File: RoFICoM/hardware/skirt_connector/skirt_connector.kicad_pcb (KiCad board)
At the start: 2 copper layers, 25 x 25 mm, 17 parts, among them J1 Cable, J10 SENSE_1, J11 SENSE_2, J12 48V_B, J13 48V_2, J14 GND_B, J15 GND_2, J16 RX_B, J17 TX_2, J2 48V_A, J3 48V_1, J4 GND_A, J5 GND_1, J6 RX_A, J7 TX_1, J8 SENSE_A, J9 SENSE_B

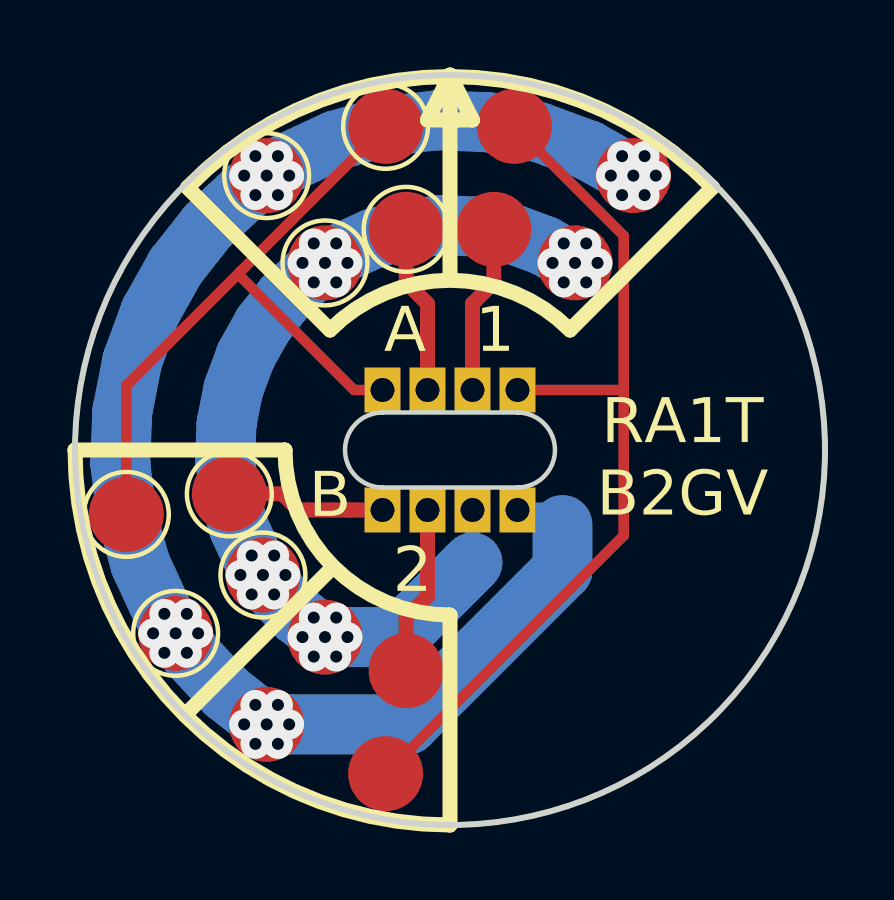
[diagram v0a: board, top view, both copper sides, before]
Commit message: RoFICoM: Add version 0.2 of the skirt PCB
- add VL53L1X distance sensor
- use flat ribbon cable for connection to the control board
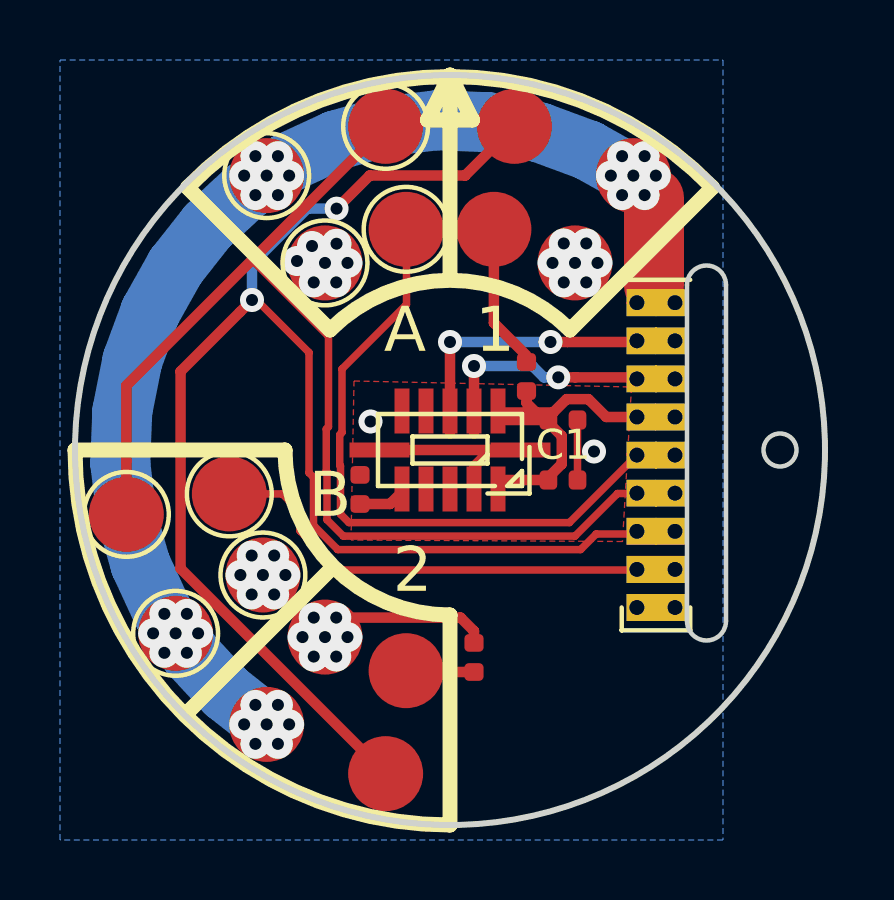
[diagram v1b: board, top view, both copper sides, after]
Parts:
- added C1: 470n, Capacitor_SMD:C_0402_1005Metric, F.Cu at (153.8, 101.0)
- added C2: 100n, Capacitor_SMD:C_0402_1005Metric, F.Cu at (153.8, 99.0)
- added R1: 10k, Resistor_SMD:R_0402_1005Metric, F.Cu at (147.0, 101.3)
- added R2: 10k, Resistor_SMD:R_0402_1005Metric, F.Cu at (152.6, 97.5)
- added R3: 10k, Resistor_SMD:R_0402_1005Metric, F.Cu at (150.8, 106.9)
- added U1: VL53L1X, rofi:VL53L1X_handsoldering, F.Cu at (150.0, 100.0)
- J1: footprint rofi:skirt_8_pin -> rofi:flat_cable_9
- moved J1 9.15 mm to (157.5, 105.2), turned to 90 degrees
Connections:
- J1 pad 1: RX -> GND
- J1 pad 2: S_A_PIN -> S_B_PIN
- J1 pad 3: S_1_PAD -> TX
- J1 pad 4: TX -> RX
- J1 pad 5: 48V -> S_A_PIN
- J1 pad 6: GND -> +3V3
- J1 pad 7: S_2_PAD -> SCL
- J1 pad 8: S_B_PIN -> SDA
- J10 pad 1: S_1_PAD -> Net-(J10-Pad1)
- J11 pad 1: S_2_PAD -> Net-(J11-Pad1)
- J12 pad 1: 48V -> +48V
- J13 pad 1: 48V -> +48V
- J2 pad 1: 48V -> +48V
- J3 pad 1: 48V -> +48V
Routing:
- net 48V: track 49.8 -> 0.00 mm, vias 28 -> 0
- net +48V: track 0.00 -> 40.2 mm, vias 0 -> 28
- net TX: track 29.9 -> 52.5 mm, vias 0 -> 2
- net GND: track 31.2 -> 13.3 mm, vias 28 -> 30
- net S_A_PIN: track 5.65 -> 22.8 mm
- net RX: track 23.0 -> 38.8 mm
- net +3V3: track 0.00 -> 13.0 mm
- net S_B_PIN: track 5.33 -> 17.5 mm
- net SDA: track 0.00 -> 11.7 mm, vias 0 -> 2
- net SCL: track 0.00 -> 10.3 mm, vias 0 -> 2
- net S_1_PAD: track 5.65 -> 0.00 mm
- net S_2_PAD: track 5.65 -> 0.00 mm
- net Net-(J10-Pad1): track 0.00 -> 4.66 mm
- net Net-(J11-Pad1): track 0.00 -> 2.40 mm
- net Net-(R1-Pad1): track 0.00 -> 1.57 mm
- added copper zone on B.Cu, net GND
- added copper zone on F.Cu, net GND
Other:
- outline, holes or cut-outs redrawn
- board text removed: "RA1T B2GV"

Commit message: RoFICoM: Update skirt connector label
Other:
- board text added: "RoFICoM Skirt v0.2 03/2019"
- board text removed: "RoFI - DockSkirt v0.1 12/2018"
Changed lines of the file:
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@@
   (gr_line (start 157.9 94.5) (end 157.9 105.7) (layer Edge.Cuts) (width 0.15))
   (gr_arc (start 158.55 94.5) (end 159.2 94.5) (angle -180) (layer Edge.Cuts) (width 0.15))
-  (gr_text "RoFI - DockSkirt\nv0.1    12/2018" (at 150.25 105.5) (layer B.SilkS)
+  (gr_text "RoFICoM Skirt\nv0.2 03/2019" (at 146.55 100.15) (layer B.SilkS)
     (effects (font (size 1.5 1.5) (thickness 0.3)) (justify mirror))
   )

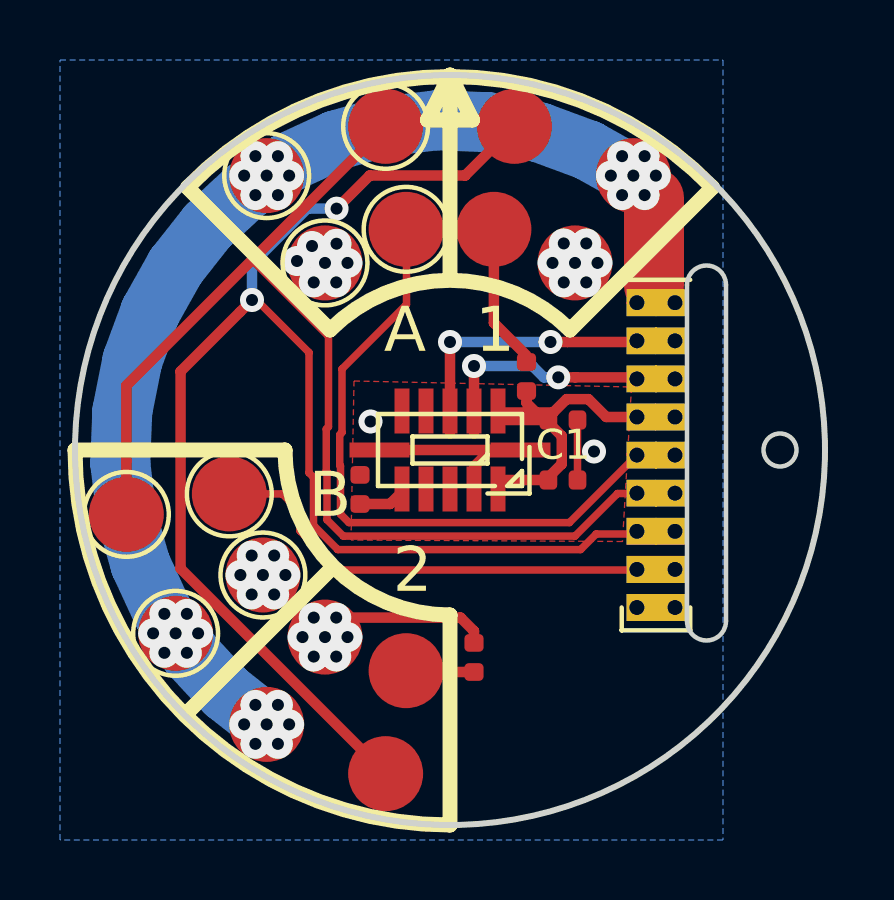
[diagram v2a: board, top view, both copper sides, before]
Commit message: RoFICoM: Add missing order codes for the skirt connector
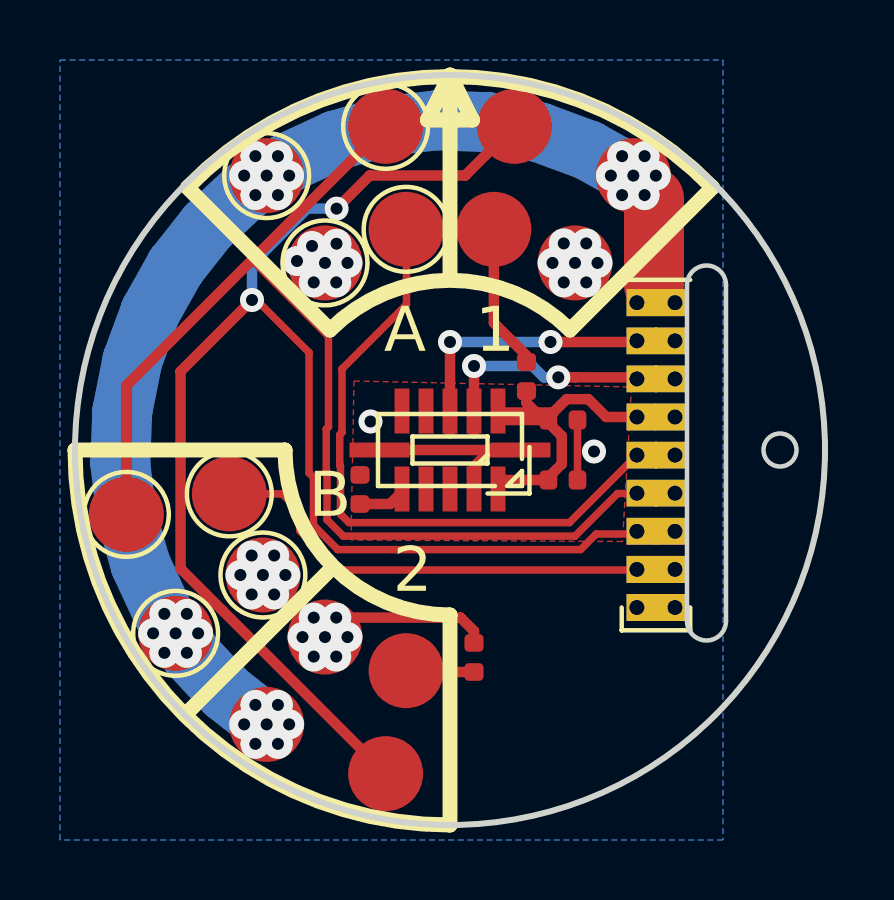
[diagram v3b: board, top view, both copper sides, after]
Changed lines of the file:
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@@
-(kicad_pcb (version 20171130) (host pcbnew 5.0.2-bee76a0~70~ubuntu18.04.1)
+(kicad_pcb (version 20171130) (host pcbnew 5.1.0-060a0da~80~ubuntu18.04.1)
   (general
     (thickness 1.6)
@@
   )
   (setup
-    (last_trace_width 0.35)
+    (last_trace_width 0.25)
     (user_trace_width 0.35)
     (user_trace_width 0.5)
@@
     (zone_45_only no)
     (trace_min 0.2)
-    (segment_width 0.5)
-    (edge_width 0.15)
     (via_size 0.8)
     (via_drill 0.4)
@@
     (uvia_min_size 0.2)
     (uvia_min_drill 0.1)
+    (edge_width 0.15)
+    (segment_width 0.5)
     (pcb_text_width 0.3)
     (pcb_text_size 1.5 1.5)
@@
     (tags capacitor)
     (attr smd)
-    (fp_text reference C1 (at 0 -1.17) (layer F.SilkS)
+    (fp_text reference C1 (at 0 -1.17) (layer F.SilkS) hide
       (effects (font (size 1 1) (thickness 0.15)))
     )
@@
   (gr_arc (start 147.039376 97.633074) (end 138.843834 107.400141) (angle -35) (layer Eco1.User) (width 0.2))
   (gr_arc (start 147.039376 97.633074) (end 137.272309 89.437532) (angle -35) (layer Eco1.User) (width 0.2))
-  (via (at 143.888727 109.146165) (size 1) (layers F.Cu B.Cu) (net 6))
-  (via (at 144.638727 109.146165) (size 1) (layers F.Cu B.Cu) (net 6))
-  (via (at 144.263727 109.795684) (size 1) (layers F.Cu B.Cu) (net 6))
-  (via (at 143.513727 109.795684) (size 1) (layers F.Cu B.Cu) (net 6))
-  (via (at 143.138727 109.146165) (size 1) (layers F.Cu B.Cu) (net 6))
-  (via (at 143.513727 108.496645) (size 1) (layers F.Cu B.Cu) (net 6))
-  (via (at 144.263727 108.496645) (size 1) (layers F.Cu B.Cu) (net 6))
-  (via (at 140.853834 106.111272) (size 1) (layers F.Cu B.Cu) (net 6))
-  (via (at 141.603834 106.111272) (size 1) (layers F.Cu B.Cu) (net 6))
-  (via (at 141.228834 106.760791) (size 1) (layers F.Cu B.Cu) (net 6))
-  (via (at 140.478834 106.760791) (size 1) (layers F.Cu B.Cu) (net 6))
-  (via (at 140.103834 106.111272) (size 1) (layers F.Cu B.Cu) (net 6))
-  (via (at 140.478834 105.461752) (size 1) (layers F.Cu B.Cu) (net 6))
-  (via (at 141.228834 105.461752) (size 1) (layers F.Cu B.Cu) (net 6))
-  (via (at 156.111272 90.853834) (size 1) (layers F.Cu B.Cu) (net 6))
-  (via (at 156.861272 90.853834) (size 1) (layers F.Cu B.Cu) (net 6))
-  (via (at 156.486272 91.503353) (size 1) (layers F.Cu B.Cu) (net 6))
-  (via (at 155.736272 91.503353) (size 1) (layers F.Cu B.Cu) (net 6))
-  (via (at 155.361272 90.853834) (size 1) (layers F.Cu B.Cu) (net 6))
-  (via (at 155.736272 90.204314) (size 1) (layers F.Cu B.Cu) (net 6))
-  (via (at 156.486272 90.204314) (size 1) (layers F.Cu B.Cu) (net 6))
-  (via (at 143.888727 90.853834) (size 1) (layers F.Cu B.Cu) (net 6))
-  (via (at 144.638727 90.853834) (size 1) (layers F.Cu B.Cu) (net 6))
-  (via (at 144.263727 91.503353) (size 1) (layers F.Cu B.Cu) (net 6))
-  (via (at 143.513727 91.503353) (size 1) (layers F.Cu B.Cu) (net 6))
-  (via (at 143.138727 90.853834) (size 1) (layers F.Cu B.Cu) (net 6))
-  (via (at 143.513727 90.204314) (size 1) (layers F.Cu B.Cu) (net 6))
-  (via (at 144.263727 90.204314) (size 1) (layers F.Cu B.Cu) (net 6))
-  (segment (start 156.111272 90.853834) (end 154.605257 90.010425) (width 2) (layer B.Cu) (net 6))
-  (segment (start 154.605257 90.010425) (end 152.985844 89.412992) (width 2) (layer B.Cu) (net 6))
-  (segment (start 152.985844 89.412992) (end 151.292911 89.076246) (width 2) (layer B.Cu) (net 6))
-  (segment (start 151.292911 89.076246) (end 149.568142 89.00848) (width 2) (layer B.Cu) (net 6))
-  (segment (start 149.568142 89.00848) (end 147.854006 89.211361) (width 2) (layer B.Cu) (net 6))
-  (segment (start 147.854006 89.211361) (end 146.192712 89.679895) (width 2) (layer B.Cu) (net 6))
-  (segment (start 146.192712 89.679895) (end 144.625166 90.402543) (width 2) (layer B.Cu) (net 6))
-  (segment (start 144.625166 90.402543) (end 143.189966 91.361513) (width 2) (layer B.Cu) (net 6))
-  (segment (start 143.189966 91.361513) (end 141.922452 92.533191) (width 2) (layer B.Cu) (net 6))
-  (segment (start 141.922452 92.533191) (end 140.853834 93.888727) (width 2) (layer B.Cu) (net 6))
-  (segment (start 140.853834 93.888727) (end 140.010425 95.394742) (width 2) (layer B.Cu) (net 6))
-  (segment (start 140.010425 95.394742) (end 139.412992 97.014155) (width 2) (layer B.Cu) (net 6))
-  (segment (start 139.076246 98.707088) (end 139.00848 100.431857) (width 2) (layer B.Cu) (net 6))
-  (segment (start 139.00848 100.431857) (end 139.211361 102.145993) (width 2) (layer B.Cu) (net 6))
-  (segment (start 139.211361 102.145993) (end 139.679895 103.807287) (width 2) (layer B.Cu) (net 6))
-  (segment (start 139.679895 103.807287) (end 140.402543 105.374833) (width 2) (layer B.Cu) (net 6))
-  (segment (start 140.402543 105.374833) (end 141.361513 106.810033) (width 2) (layer B.Cu) (net 6))
-  (segment (start 141.361513 106.810033) (end 142.533191 108.077547) (width 2) (layer B.Cu) (net 6))
-  (segment (start 142.533191 108.077547) (end 143.888727 109.146165) (width 2) (layer B.Cu) (net 6))
-  (segment (start 139.412992 97.014155) (end 139.076246 98.707088) (width 2) (layer B.Cu) (net 6))
   (via (at 145.833223 106.236022) (size 1) (layers F.Cu B.Cu) (net 1))
   (via (at 146.583223 106.236022) (size 1) (layers F.Cu B.Cu) (net 1))
@@
   (segment (start 152.145993 89.211361) (end 150.507354 90.85) (width 0.35) (layer F.Cu) (net 5))
   (segment (start 150.507354 90.85) (end 147.323891 90.85) (width 0.35) (layer F.Cu) (net 5))
+  (via (at 143.888727 109.146165) (size 1) (layers F.Cu B.Cu) (net 6))
+  (via (at 144.638727 109.146165) (size 1) (layers F.Cu B.Cu) (net 6))
+  (via (at 144.263727 109.795684) (size 1) (layers F.Cu B.Cu) (net 6))
+  (via (at 143.513727 109.795684) (size 1) (layers F.Cu B.Cu) (net 6))
+  (via (at 143.138727 109.146165) (size 1) (layers F.Cu B.Cu) (net 6))
+  (via (at 143.513727 108.496645) (size 1) (layers F.Cu B.Cu) (net 6))
+  (via (at 144.263727 108.496645) (size 1) (layers F.Cu B.Cu) (net 6))
+  (via (at 140.853834 106.111272) (size 1) (layers F.Cu B.Cu) (net 6))
+  (via (at 141.603834 106.111272) (size 1) (layers F.Cu B.Cu) (net 6))
+  (via (at 141.228834 106.760791) (size 1) (layers F.Cu B.Cu) (net 6))
+  (via (at 140.478834 106.760791) (size 1) (layers F.Cu B.Cu) (net 6))
+  (via (at 140.103834 106.111272) (size 1) (layers F.Cu B.Cu) (net 6))
+  (via (at 140.478834 105.461752) (size 1) (layers F.Cu B.Cu) (net 6))
+  (via (at 141.228834 105.461752) (size 1) (layers F.Cu B.Cu) (net 6))
+  (via (at 156.111272 90.853834) (size 1) (layers F.Cu B.Cu) (net 6))
+  (via (at 156.861272 90.853834) (size 1) (layers F.Cu B.Cu) (net 6))
+  (via (at 156.486272 91.503353) (size 1) (layers F.Cu B.Cu) (net 6))
+  (via (at 155.736272 91.503353) (size 1) (layers F.Cu B.Cu) (net 6))
+  (via (at 155.361272 90.853834) (size 1) (layers F.Cu B.Cu) (net 6))
+  (via (at 155.736272 90.204314) (size 1) (layers F.Cu B.Cu) (net 6))
+  (via (at 156.486272 90.204314) (size 1) (layers F.Cu B.Cu) (net 6))
+  (via (at 143.888727 90.853834) (size 1) (layers F.Cu B.Cu) (net 6))
+  (via (at 144.638727 90.853834) (size 1) (layers F.Cu B.Cu) (net 6))
+  (via (at 144.263727 91.503353) (size 1) (layers F.Cu B.Cu) (net 6))
+  (via (at 143.513727 91.503353) (size 1) (layers F.Cu B.Cu) (net 6))
+  (via (at 143.138727 90.853834) (size 1) (layers F.Cu B.Cu) (net 6))
+  (via (at 143.513727 90.204314) (size 1) (layers F.Cu B.Cu) (net 6))
+  (via (at 144.263727 90.204314) (size 1) (layers F.Cu B.Cu) (net 6))
+  (segment (start 156.111272 90.853834) (end 154.605257 90.010425) (width 2) (layer B.Cu) (net 6))
+  (segment (start 154.605257 90.010425) (end 152.985844 89.412992) (width 2) (layer B.Cu) (net 6))
+  (segment (start 152.985844 89.412992) (end 151.292911 89.076246) (width 2) (layer B.Cu) (net 6))
+  (segment (start 151.292911 89.076246) (end 149.568142 89.00848) (width 2) (layer B.Cu) (net 6))
+  (segment (start 149.568142 89.00848) (end 147.854006 89.211361) (width 2) (layer B.Cu) (net 6))
+  (segment (start 147.854006 89.211361) (end 146.192712 89.679895) (width 2) (layer B.Cu) (net 6))
+  (segment (start 146.192712 89.679895) (end 144.625166 90.402543) (width 2) (layer B.Cu) (net 6))
+  (segment (start 144.625166 90.402543) (end 143.189966 91.361513) (width 2) (layer B.Cu) (net 6))
+  (segment (start 143.189966 91.361513) (end 141.922452 92.533191) (width 2) (layer B.Cu) (net 6))
+  (segment (start 141.922452 92.533191) (end 140.853834 93.888727) (width 2) (layer B.Cu) (net 6))
+  (segment (start 140.853834 93.888727) (end 140.010425 95.394742) (width 2) (layer B.Cu) (net 6))
+  (segment (start 140.010425 95.394742) (end 139.412992 97.014155) (width 2) (layer B.Cu) (net 6))
+  (segment (start 139.076246 98.707088) (end 139.00848 100.431857) (width 2) (layer B.Cu) (net 6))
+  (segment (start 139.00848 100.431857) (end 139.211361 102.145993) (width 2) (layer B.Cu) (net 6))
+  (segment (start 139.211361 102.145993) (end 139.679895 103.807287) (width 2) (layer B.Cu) (net 6))
+  (segment (start 139.679895 103.807287) (end 140.402543 105.374833) (width 2) (layer B.Cu) (net 6))
+  (segment (start 140.402543 105.374833) (end 141.361513 106.810033) (width 2) (layer B.Cu) (net 6))
+  (segment (start 141.361513 106.810033) (end 142.533191 108.077547) (width 2) (layer B.Cu) (net 6))
+  (segment (start 142.533191 108.077547) (end 143.888727 109.146165) (width 2) (layer B.Cu) (net 6))
+  (segment (start 139.412992 97.014155) (end 139.076246 98.707088) (width 2) (layer B.Cu) (net 6))
   (segment (start 156.23 95.09) (end 156.8 94.52) (width 0.7) (layer F.Cu) (net 6))
   (segment (start 156.8 94.52) (end 156.92 94.52) (width 0.35) (layer F.Cu) (net 6))

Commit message: RoFICoM: Move cable to the bottom side of skirt connector
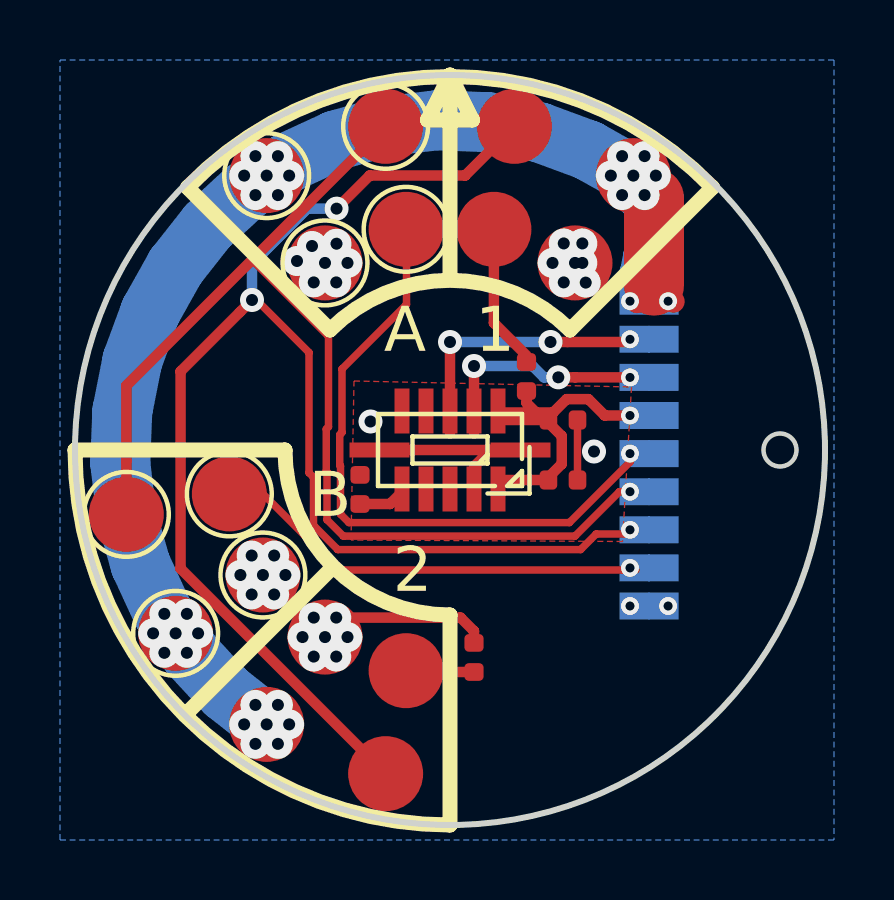
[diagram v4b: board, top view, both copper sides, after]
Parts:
- J1: footprint rofi:flat_cable_9 -> rofi:flat_cable_9_smd; moved to B.Cu
- R1, R2, R3: value 10k -> 100k
- moved J1 1.50 mm to (156.0, 105.2)
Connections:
- U1 pad 7: Net-(U1-Pad7) -> (no net)
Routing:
- net +48V: track 40.2 -> 45.2 mm, vias 28 -> 30
- net S_B_PIN: track 17.5 -> 15.9 mm, vias 0 -> 1
- net SCL: track 10.3 -> 8.88 mm, vias 2 -> 3
- net SDA: track 11.7 -> 10.4 mm, vias 2 -> 3
- net GND: track 13.3 -> 14.6 mm, vias 30 -> 32
- net RX: track 38.8 -> 38.5 mm, vias 0 -> 1
- net +3V3: track 13.0 -> 12.8 mm, vias 0 -> 1
- net S_A_PIN: track 22.8 -> 22.6 mm, vias 0 -> 1
- net TX: track 52.5 -> 52.4 mm, vias 2 -> 3
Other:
- outline, holes or cut-outs redrawn
